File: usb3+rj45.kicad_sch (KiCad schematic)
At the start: 63 parts, among them J1 Amphenol_RJE361882415, T1 Choke_SRF2012A-801Y, T2 Choke_SRF2012A-801Y, T3 Choke_SRF2012A-801Y, T4 Choke_SRF2012A-801Y, T5 Trans_SM453229-381N7Y, T6 Trans_SM453229-381N7Y, T7 Trans_SM453229-381N7Y, T8 Trans_SM453229-381N7Y, U1 ESD204DQAR, U2 ESD204DQAR, U3 AP22615A_TSOT26, U4 AP22615A_TSOT26

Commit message: [#70030] Unify functional block names
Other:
- company: Antmicro Ltd. -> Antmicro Ltd
- title: Com Express 7 baseboard -> COM Express 7 Baseboard
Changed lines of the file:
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@@
 	(paper "A3")
 	(title_block
-		(title "Com Express 7 baseboard")
-		(date "2024-03-28")
+		(title "COM Express 7 Baseboard")
+		(date "2024-12-13")
 		(rev "1.1.0")
-		(company "Antmicro Ltd.")
+		(company "Antmicro Ltd")
+		(comment 1 "www.antmicro.com")
 	)
 	(junction

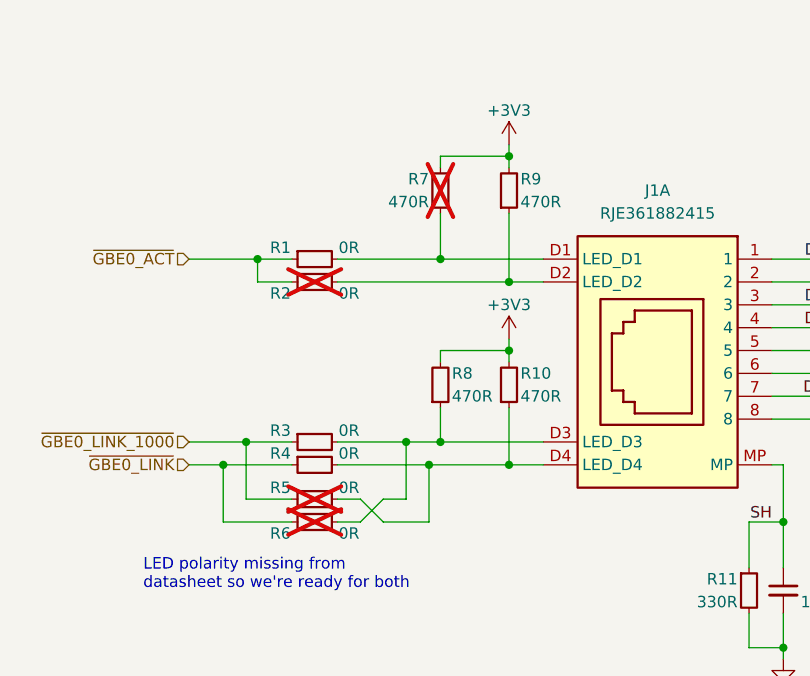
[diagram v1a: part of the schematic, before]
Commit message: [#70532] Fix RJ45 LEDs connection
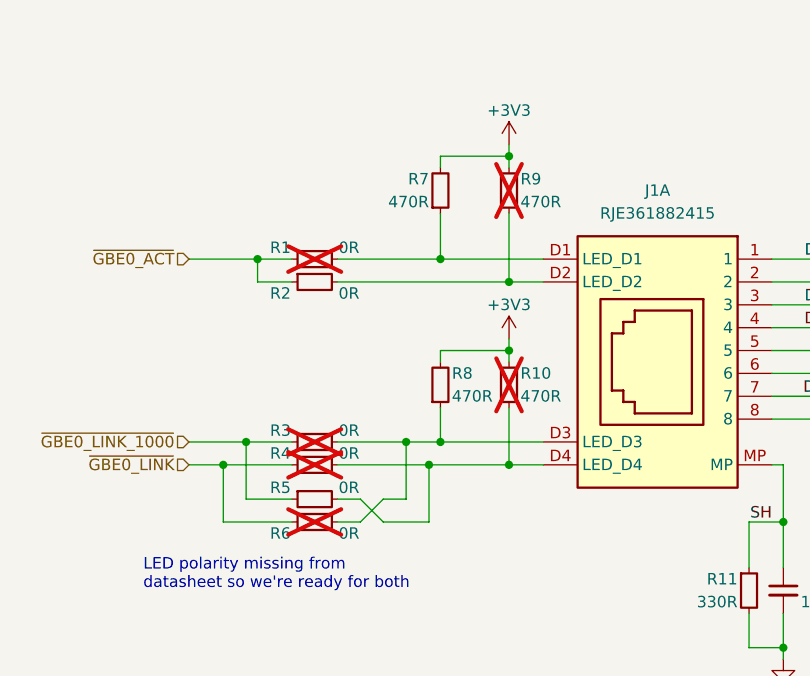
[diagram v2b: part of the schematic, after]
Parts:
- R1, R10, R3, R4, R9: now not fitted
- R2, R5, R7: now fitted
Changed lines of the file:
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@@
 		(in_bom yes)
 		(on_board yes)
-		(dnp no)
+		(dnp yes)
 		(property "Reference" "R4"
 			(at 107.95 85.09 0)
@@
 		(in_bom yes)
 		(on_board yes)
-		(dnp no)
+		(dnp yes)
 		(property "Reference" "R9"
 			(at 134.62 54.61 90)
@@
 		(in_bom yes)
 		(on_board yes)
-		(dnp yes)
+		(dnp no)
 		(property "Reference" "R7"
 			(at 124.46 54.61 90)
@@
 		(in_bom yes)
 		(on_board yes)
-		(dnp yes)
+		(dnp no)
 		(property "Reference" "R5"
 			(at 107.95 88.9 0)
@@
 		(in_bom yes)
 		(on_board yes)
-		(dnp no)
+		(dnp yes)
 		(property "Reference" "R10"
 			(at 134.62 76.2 90)
@@
 		(in_bom yes)
 		(on_board yes)
-		(dnp yes)
+		(dnp no)
 		(property "Reference" "R2"
 			(at 107.95 67.31 0)
@@
 		(in_bom yes)
 		(on_board yes)
-		(dnp no)
+		(dnp yes)
 		(property "Reference" "R3"
 			(at 107.95 82.55 0)
@@
 		(in_bom yes)
 		(on_board yes)
-		(dnp no)
+		(dnp yes)
 		(property "Reference" "R1"
 			(at 107.95 62.23 0)

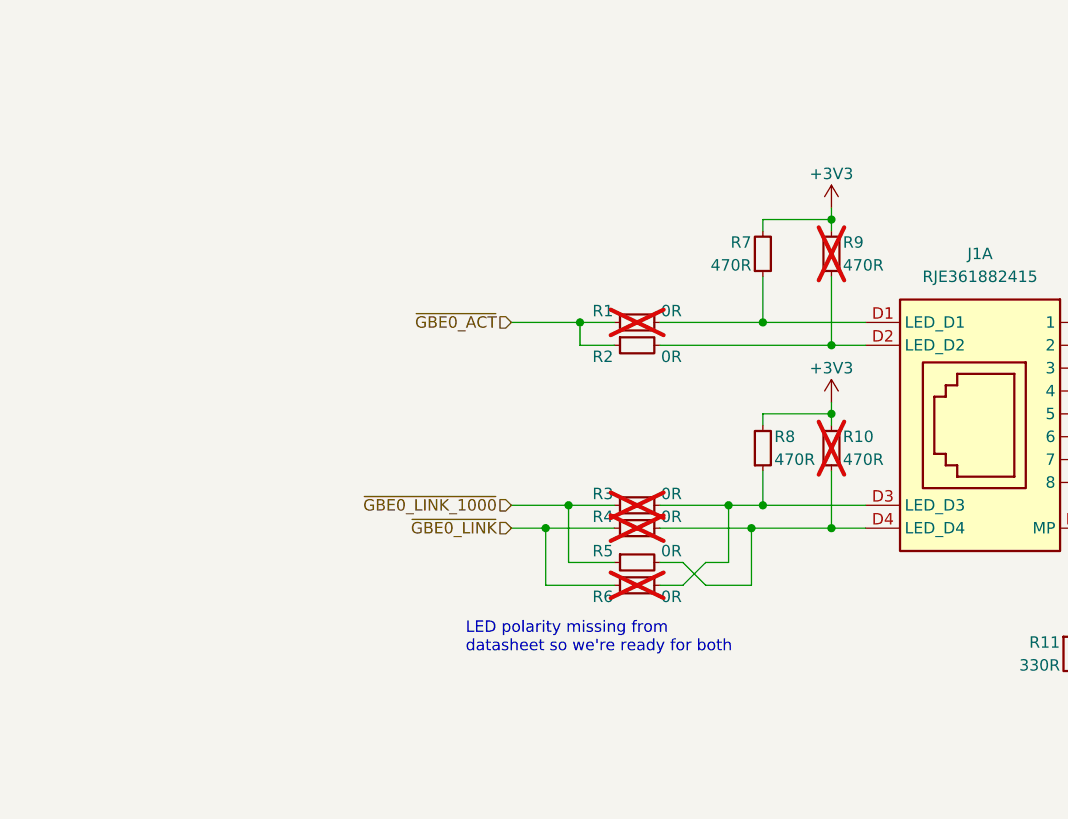
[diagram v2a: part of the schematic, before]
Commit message: [#70532] Fix RJ45 GBE0_ACT LED logic
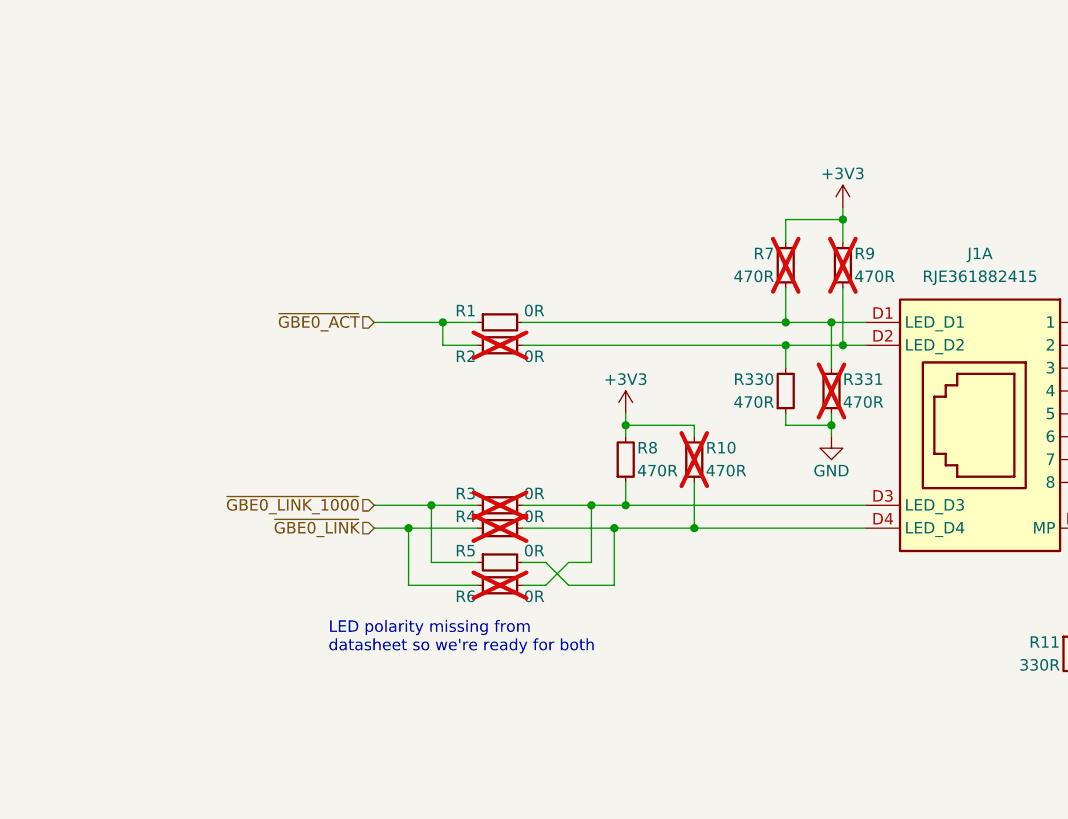
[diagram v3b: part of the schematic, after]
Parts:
- added R330, R331: R_470R_0402, antmicro-footprints:R_0402_1005Metric, symbol antmicroResistors0402:R_470R_0402
- R1: now fitted
- R2, R7: now not fitted
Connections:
- net GND: now also R330.1, R331.1
- net at J1.D2 (LED_D2), R2.2, R9.1: now also R330.2
- net at J1.D1 (LED_D1), R1.2, R7.1: now also R331.2
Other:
- moved on the sheet: R10, R3, R4, R5, R6, R8, R9

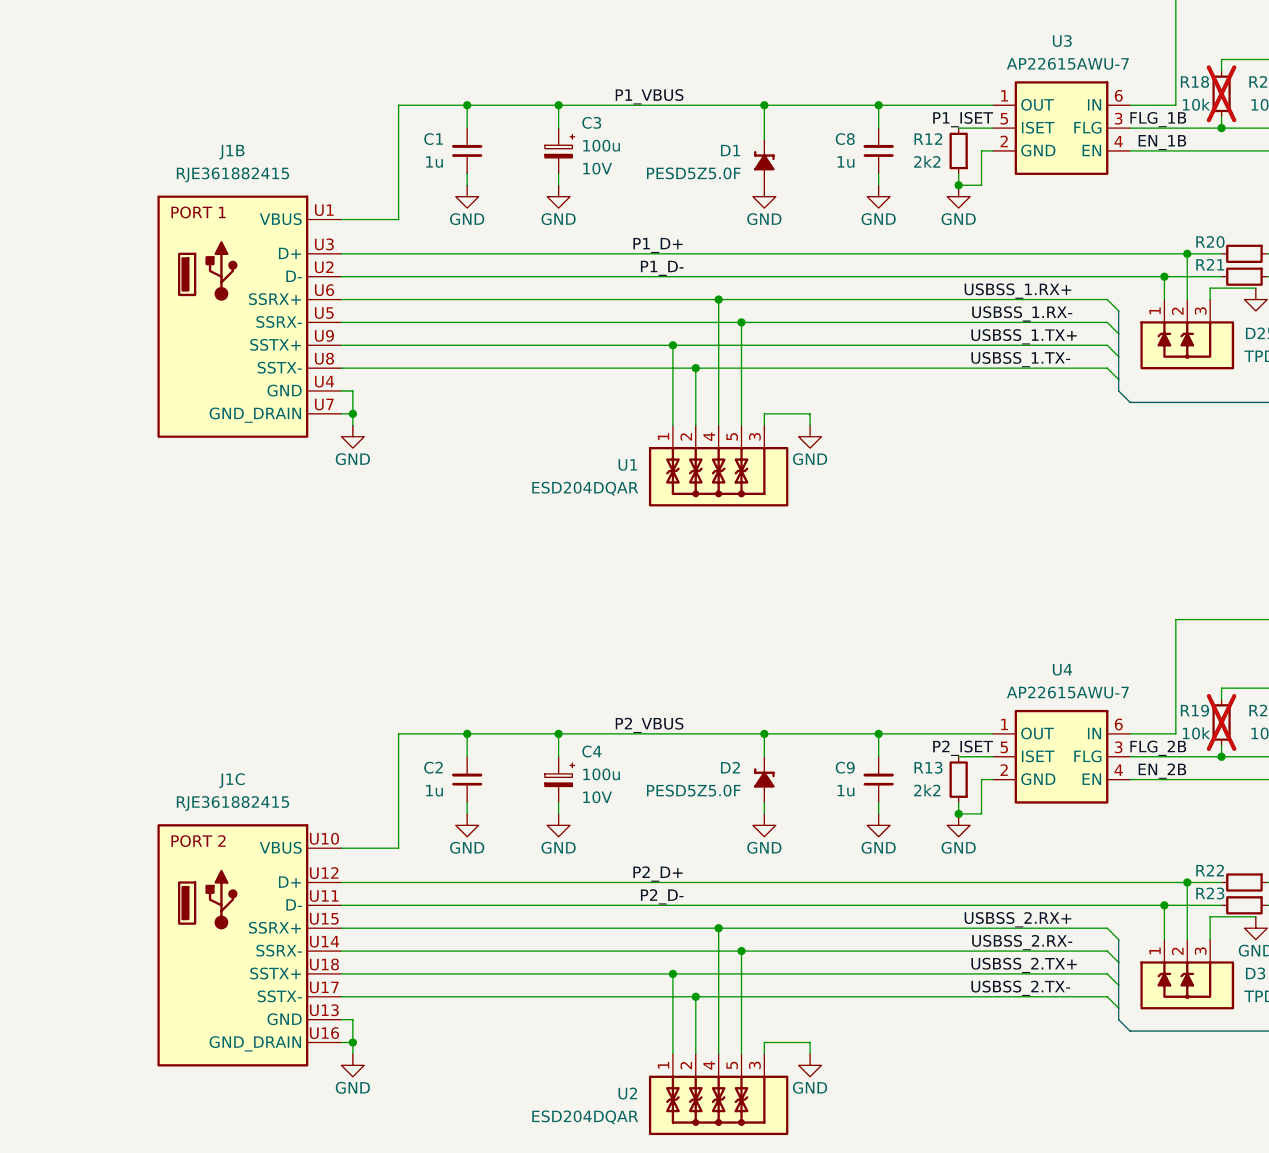
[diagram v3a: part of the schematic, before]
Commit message: [#70532] Fix USB SS pinout (J1)
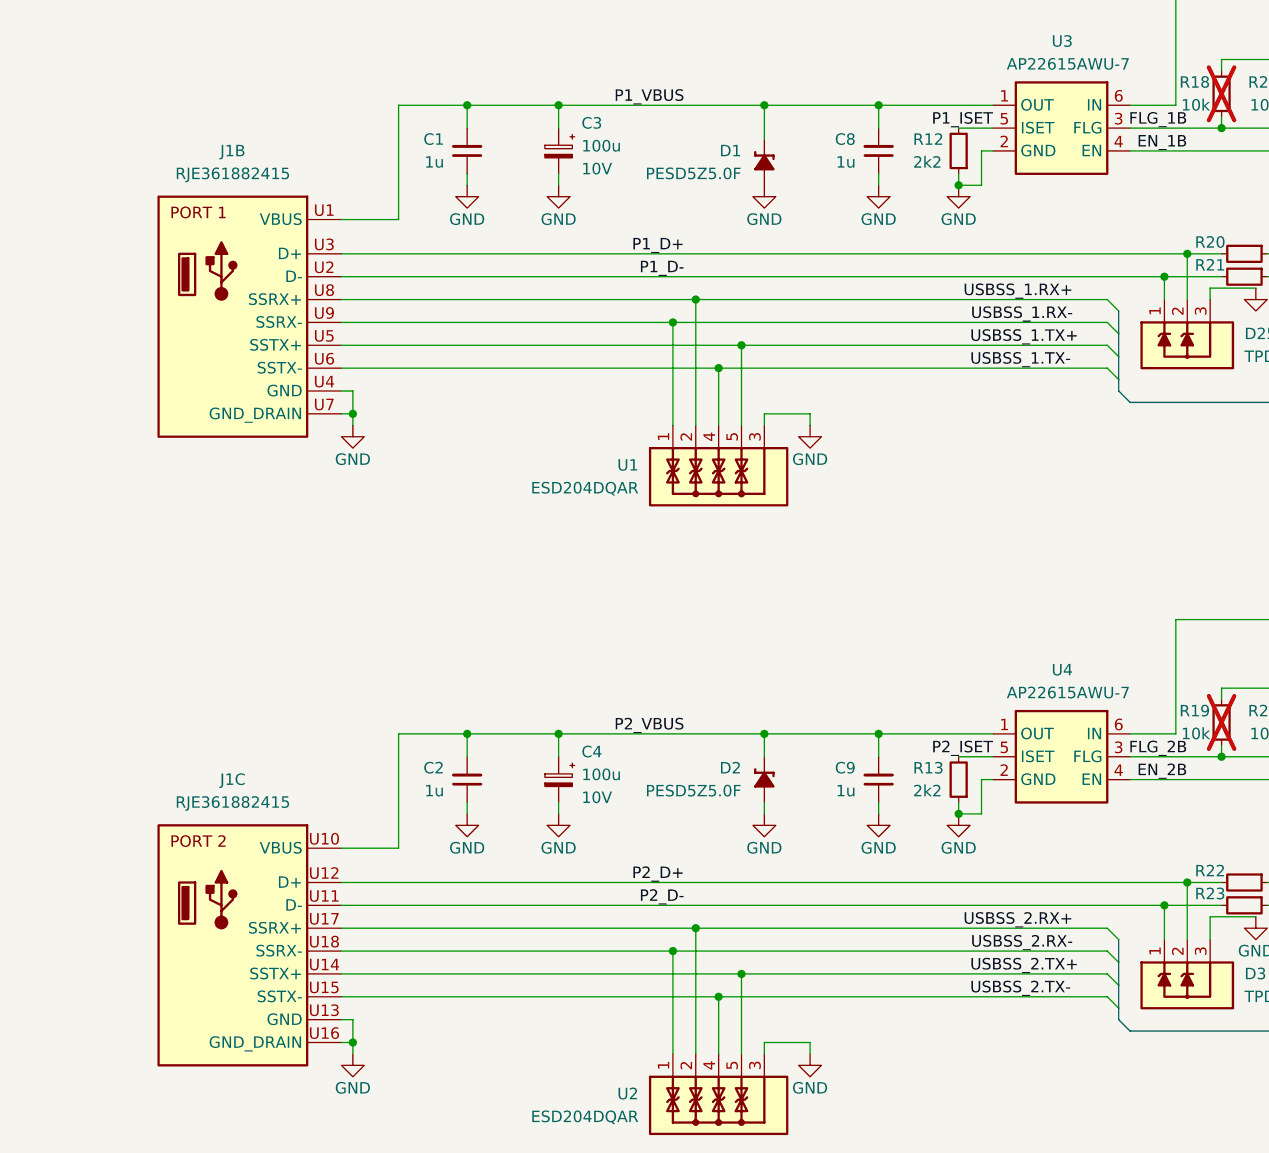
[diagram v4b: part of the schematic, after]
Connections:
- net USBSS_1.RX+: now also J1.U8 (SSRX+), U1.2, U1.9; no longer J1.U6 (SSRX+), U1.4, U1.7
- net USBSS_1.RX-: now also J1.U9 (SSRX-), U1.1, U1.10; no longer J1.U5 (SSRX-), U1.5, U1.6
- net USBSS_1.TX+: now also J1.U5 (SSTX+), U1.5, U1.6; no longer J1.U9 (SSTX+), U1.1, U1.10
- net USBSS_1.TX-: now also J1.U6 (SSTX-), U1.4, U1.7; no longer J1.U8 (SSTX-), U1.2, U1.9
- net USBSS_2.RX+: now also J1.U17 (SSRX+), U2.2, U2.9; no longer J1.U15 (SSRX+), U2.4, U2.7
- net USBSS_2.RX-: now also J1.U18 (SSRX-), U2.1, U2.10; no longer J1.U14 (SSRX-), U2.5, U2.6
- net USBSS_2.TX+: now also J1.U14 (SSTX+), U2.5, U2.6; no longer J1.U18 (SSTX+), U2.1, U2.10
- net USBSS_2.TX-: now also J1.U15 (SSTX-), U2.4, U2.7; no longer J1.U17 (SSTX-), U2.2, U2.9
